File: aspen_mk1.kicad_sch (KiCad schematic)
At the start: 150 parts, among them SW1 SW_Push, SW10 SW_Push, SW11 SW_Push, SW12 SW_Push, SW13 SW_Push, SW14 SW_Push, SW15 SW_Push, SW16 SW_Push, SW17 SW_Push, SW18 SW_Push, SW19 SW_Push, SW2 SW_Push, SW20 SW_Push, SW21 SW_Push, SW22 SW_Push, SW23 SW_Push, SW24 SW_Push, SW25 SW_Push, SW26 SW_Push, SW27 SW_Push, SW28 SW_Push, SW29 SW_Push, SW3 SW_Push, SW30 SW_Push, SW31 SW_Push, SW32 SW_Push, SW33 SW_Push, SW34 SW_Push, SW35 SW_Push, SW36 SW_Push, SW37 SW_Push, SW38 SW_Push, SW39 SW_Push, SW4 SW_Push, SW40 SW_Push, SW41 SW_Push, SW42 SW_Push, SW43 SW_Push, SW44 SW_Push, SW45 SW_Push, SW46 SW_Push, SW47 SW_Push, SW48 SW_Push, SW49 SW_Push, SW5 SW_Push, SW50 SW_Push, SW51 SW_Push, SW52 SW_Push, SW53 SW_Push, SW54 SW_Push, SW55 SW_Push, SW56 SW_Push, SW57 SW_Push, SW58 SW_Push, SW59 SW_Push, SW6 SW_Push, SW60 SW_Push, SW61 SW_Push, SW62 SW_Push, SW63 SW_Push, SW64 SW_Push, SW65 SW_Push, SW66 SW_Push, SW67 SW_Push, SW68 SW_Push, SW7 SW_Push, SW8 SW_Push, SW9 SW_Push, U1 LD1117S33TR_SOT223, U2 STM32F042C4Tx

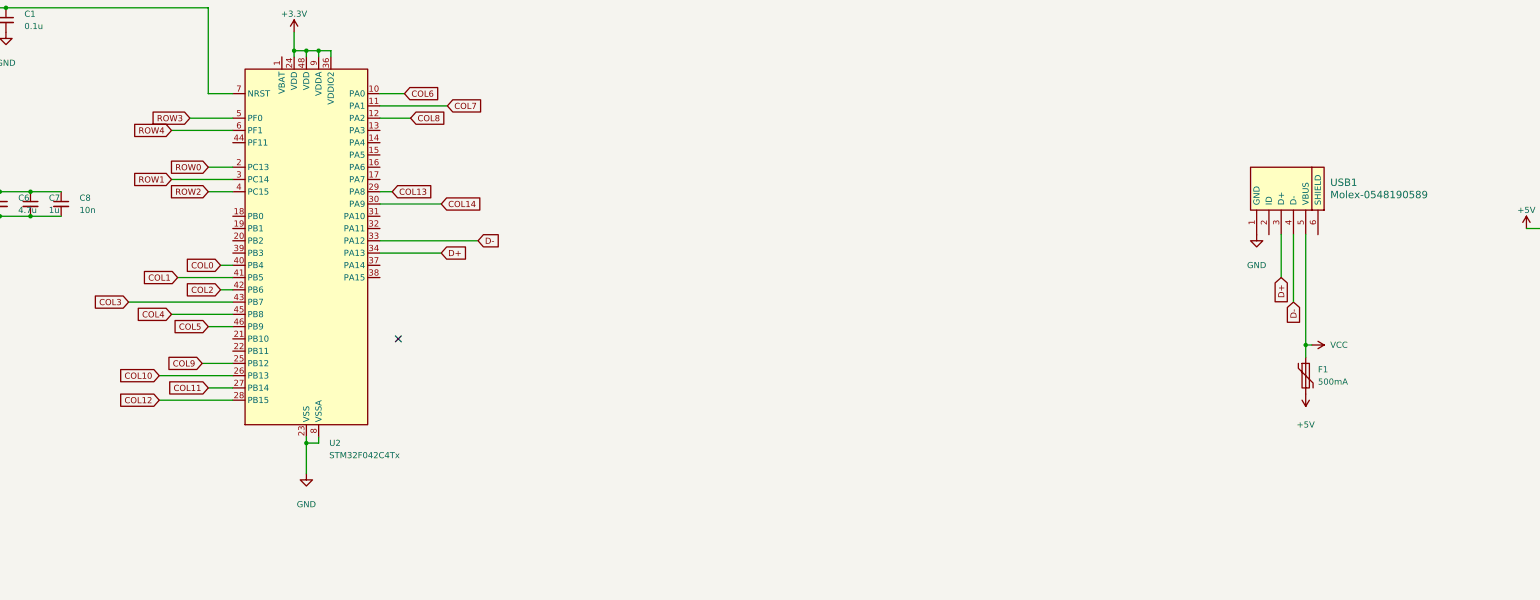
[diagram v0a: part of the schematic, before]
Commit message: remove accidental proprietary model
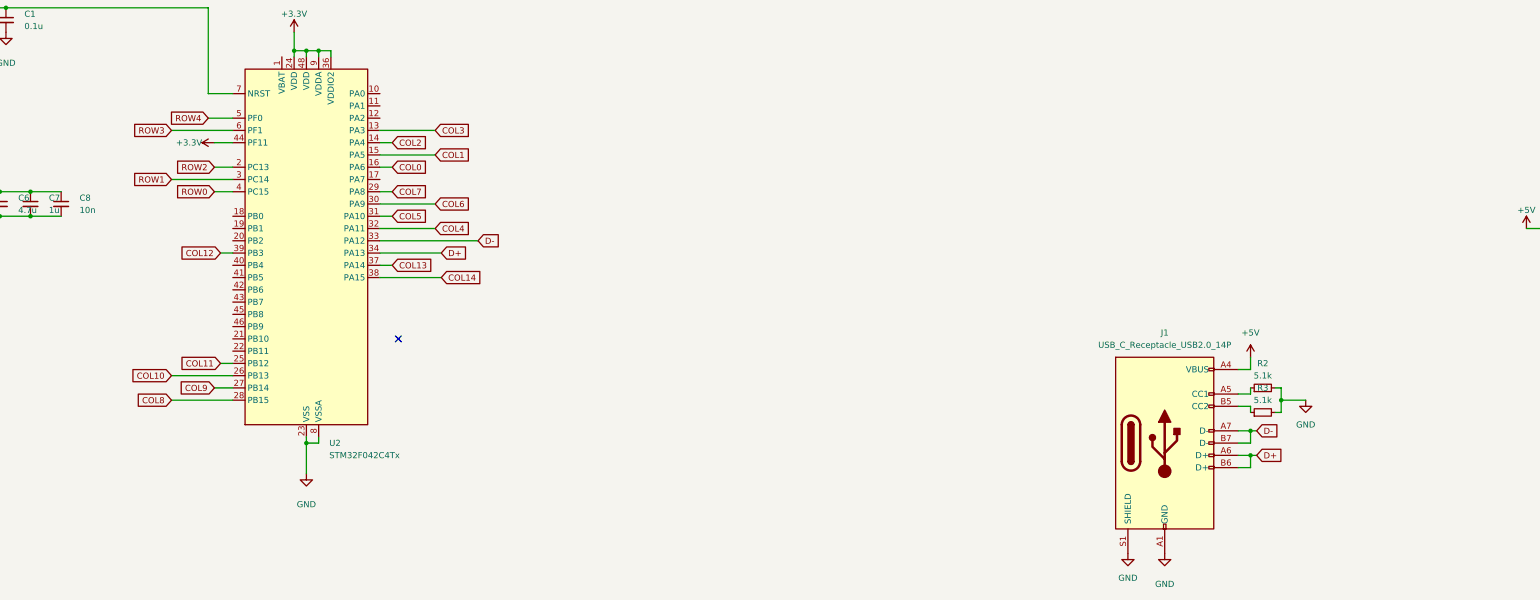
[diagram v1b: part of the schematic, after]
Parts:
- removed F1: 500mA, Fuse:Fuse_1210_3225Metric, symbol Device:Polyfuse
- removed USB1: Molex-0548190589, random-keyboard-parts:Molex-0548190589, symbol random-keyboard-parts:Molex-0548190589
- added J1: USB_C_Receptacle_USB2.0_14P, Connector_USB:USB_C_Receptacle_JAE_DX07S016JA1R1500, symbol Connector:USB_C_Receptacle_USB2.0_14P
- added R2, R3: 5.1k, Resistor_SMD:R_0805_2012Metric, symbol Device:R_Small
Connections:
- net +3.3V: now also U2.44 (PF11)
- net +5V: now also J1.A4 (VBUS), J1.A9 (VBUS), J1.B4 (VBUS), J1.B9 (VBUS)
- net COL0: now also U2.16 (PA6); no longer U2.40 (PB4)
- net COL1: now also U2.15 (PA5); no longer U2.41 (PB5)
- net COL11: now also U2.25 (PB12); no longer U2.27 (PB14)
- net COL12: now also U2.39 (PB3); no longer U2.28 (PB15)
- net COL13: now also U2.37 (PA14); no longer U2.29 (PA8)
- net COL14: now also U2.38 (PA15); no longer U2.30 (PA9)
- net COL2: now also U2.14 (PA4); no longer U2.42 (PB6)
- net COL3: now also U2.13 (PA3); no longer U2.43 (PB7)
- net COL4: now also U2.32 (PA11); no longer U2.45 (PB8)
- net COL5: now also U2.31 (PA10); no longer U2.46 (PB9)
- net COL6: now also U2.30 (PA9); no longer U2.10 (PA0)
- net COL7: now also U2.29 (PA8); no longer U2.11 (PA1)
- net COL8: now also U2.28 (PB15); no longer U2.12 (PA2)
- net COL9: now also U2.27 (PB14); no longer U2.25 (PB12)
- net D+: now also J1.A6 (D+), J1.B6 (D+)
- net D-: now also J1.A7 (D-), J1.B7 (D-)
- net GND: now also J1.A1 (GND), J1.A12 (GND), J1.B1 (GND), J1.B12 (GND), J1.S1 (SHIELD), R2.2, R3.2
- net ROW0: now also U2.4 (PC15); no longer U2.2 (PC13)
- net ROW2: now also U2.2 (PC13); no longer U2.4 (PC15)
- net ROW3: now also U2.6 (PF1); no longer U2.5 (PF0)
- net ROW4: now also U2.5 (PF0); no longer U2.6 (PF1)
- new net: J1.B5 (CC2), R3.1
- new net: J1.A5 (CC1), R2.1
